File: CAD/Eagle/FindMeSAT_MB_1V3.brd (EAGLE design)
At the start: 99 x 49.2 mm, 137 parts, among them Q101 ABS07-32.768KHZ, Q651 ABM3B-16MHZ-10-R50-1-U, U1001 CFPT-141-20MHZ, U101 ATXMEGA256A3BU-AU, U1011 OPA354, U1021 OPA354, U1111 LM2831YMF, U1121 LM4120IM5-3.0, U201 SIM808, U301 MPU-9250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

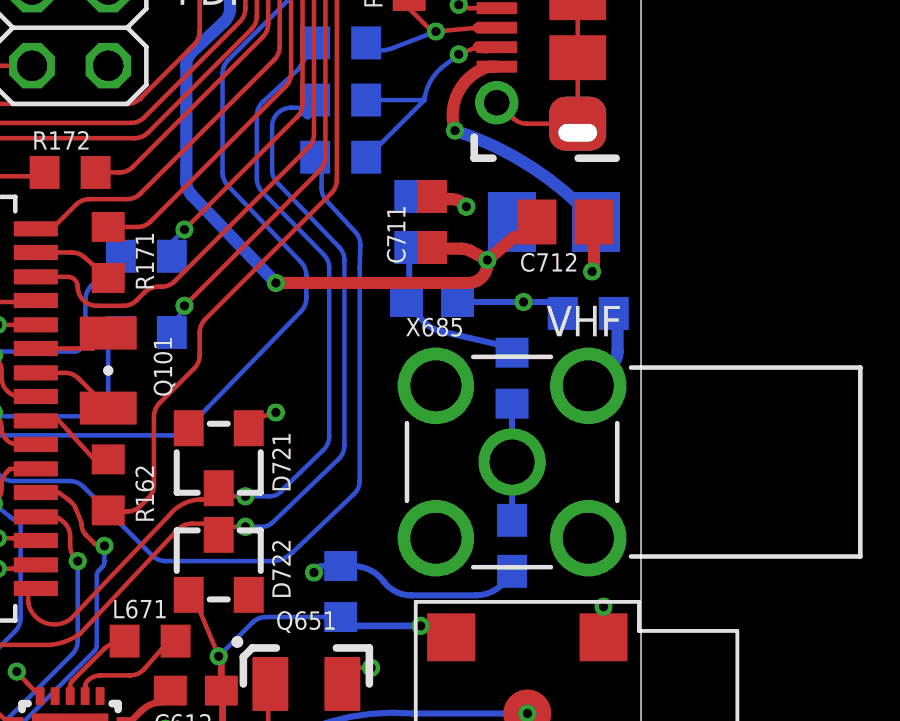
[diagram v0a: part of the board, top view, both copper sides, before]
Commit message: HW_V1.3 - L687 added, AX5243 UHF matching unit enhanced
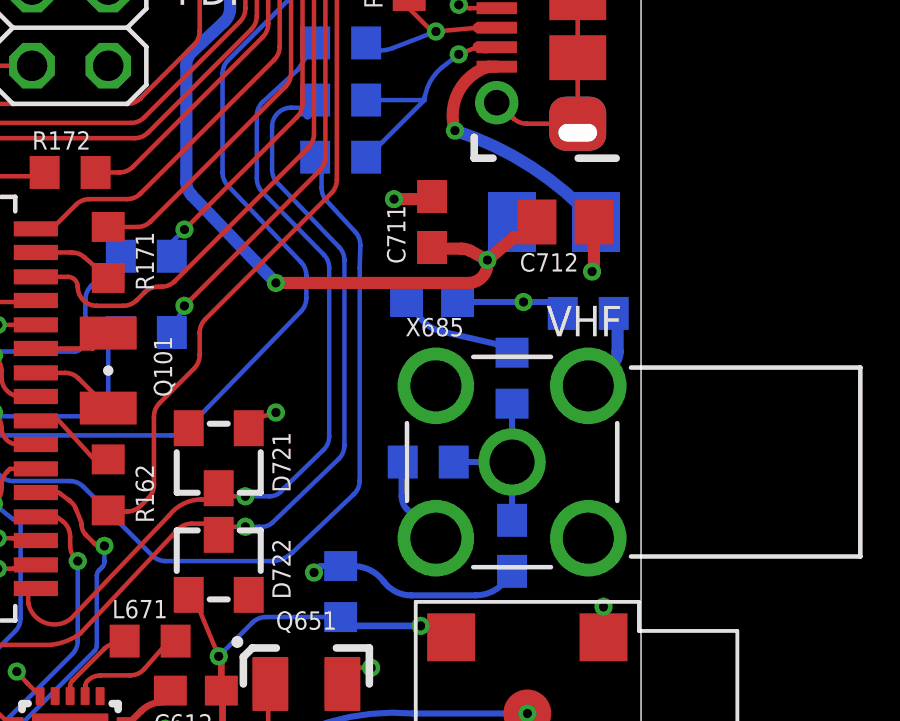
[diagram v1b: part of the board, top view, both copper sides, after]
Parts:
- removed C682: 4.7pF, rcl:C0603
- added L687: 150nH, rcl:R0603
- C681: value 33pF -> 82pF
- C686: value 4.7pF -> 150pF
- L681: value 150nH -> 100nH
- L682: value 22nH -> 56nH
- L686: value 22nH -> 33nH
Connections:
- net AX_ANT: now also L687.2
- net AX_ANT_I: no longer C682.2
- net GND: now also L687.1; no longer C682.1
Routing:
- net AX_ANT: track 3.89 -> 5.83 mm
- net AX_ANT_I: track 5.87 -> 4.14 mm
- net N$5: track 0.00 -> 1.14 mm, vias 0 -> 1
- net GND: track 234.3 -> 233.6 mm, vias 73 -> 72

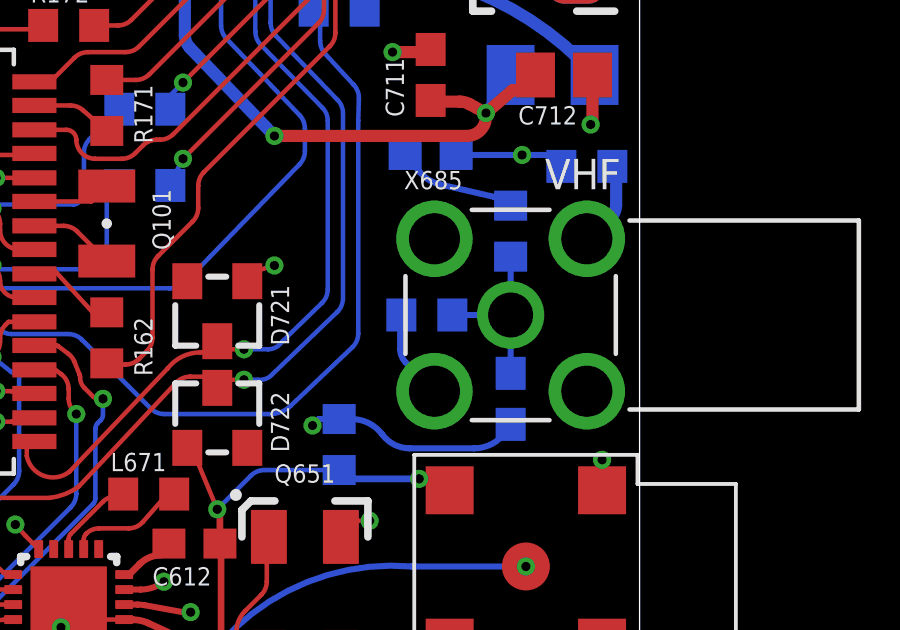
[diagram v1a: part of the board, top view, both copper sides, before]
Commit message: HW_V1.3 - AX5243 - another matching setup
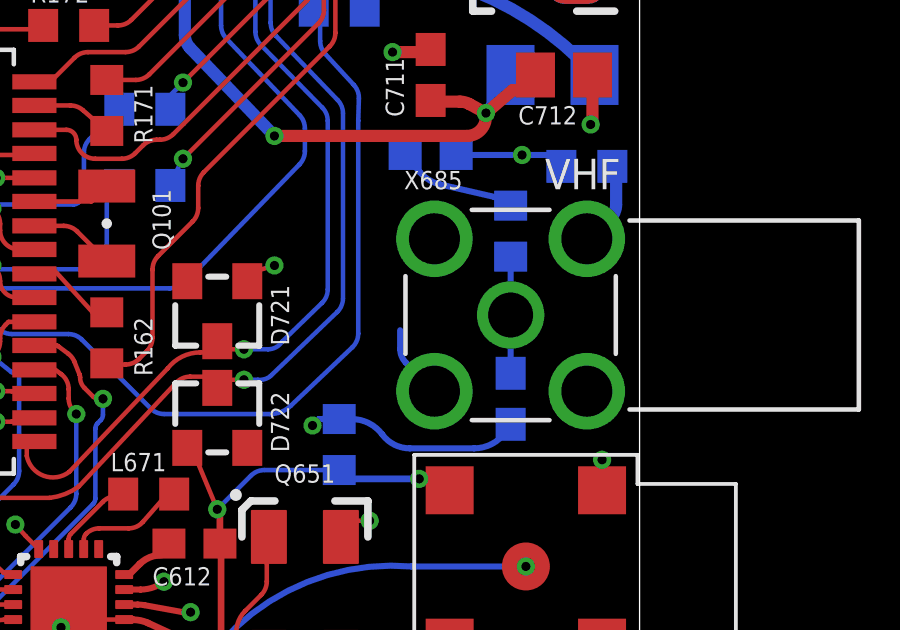
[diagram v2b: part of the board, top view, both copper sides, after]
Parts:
- removed L687: 150nH, rcl:R0603
- C681: value 82pF -> 47pF
- C686: value 150pF -> 3.9pF
- L681: value 100nH -> 150nH
- L682: value 56nH -> 47nH
- L686: value 33nH -> 18nH
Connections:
- net AX_ANT: no longer L687.2
- net GND: no longer L687.1
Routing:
- net AX_ANT: track 5.83 -> 3.89 mm
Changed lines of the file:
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@@
 <attribute name="VALUE" x="81.788" y="7.112" size="0.6096" layer="27"/>
 </element>
-<element name="C681" library="rcl" package="C0603" value="82pF" x="92.075" y="18.796" smashed="yes" rot="MR0">
+<element name="C681" library="rcl" package="C0603" value="47pF" x="92.075" y="18.796" smashed="yes" rot="MR0">
 <attribute name="NAME" x="90.17" y="18.415" size="0.6096" layer="26" rot="MR0"/>
 <attribute name="VALUE" x="92.456" y="18.542" size="0.6096" layer="28" rot="MR0"/>
 </element>
-<element name="L686" library="rcl" package="R0603" value="33nH" x="89.027" y="9.144" smashed="yes" rot="MR90">
+<element name="L686" library="rcl" package="R0603" value="18nH" x="89.027" y="9.144" smashed="yes" rot="MR90">
 <attribute name="NAME" x="88.773" y="5.207" size="0.6096" layer="26" rot="MR90"/>
 <attribute name="VALUE" x="88.773" y="8.001" size="0.6096" layer="28" rot="MR90"/>
 </element>
-<element name="L682" library="rcl" package="R0603" value="56nH" x="94.742" y="16.256" smashed="yes" rot="MR270">
+<element name="L682" library="rcl" package="R0603" value="47nH" x="94.742" y="16.256" smashed="yes" rot="MR270">
 <attribute name="NAME" x="94.488" y="18.034" size="0.6096" layer="26" rot="MR90"/>
 <attribute name="VALUE" x="94.488" y="15.24" size="0.6096" layer="28" rot="MR90"/>
 </element>
-<element name="C686" library="rcl" package="C0603" value="150pF" x="94.742" y="10.668" smashed="yes" rot="MR90">
+<element name="C686" library="rcl" package="C0603" value="3.9pF" x="94.742" y="10.668" smashed="yes" rot="MR90">
 <attribute name="NAME" x="94.488" y="6.604" size="0.6096" layer="26" rot="MR90"/>
 <attribute name="VALUE" x="94.488" y="10.287" size="0.6096" layer="28" rot="MR90"/>
 </element>
-<element name="L681" library="rcl" package="R0603" value="100nH" x="97.282" y="18.415" smashed="yes" rot="MR180">
+<element name="L681" library="rcl" package="R0603" value="150nH" x="97.282" y="18.415" smashed="yes" rot="MR180">
 <attribute name="NAME" x="98.425" y="19.304" size="0.6096" layer="26" rot="MR0"/>
 <attribute name="VALUE" x="98.552" y="18.161" size="0.6096" layer="28" rot="MR0"/>
@@
 <attribute name="VALUE" x="46.355" y="26.162" size="0.6096" layer="27" rot="R270"/>
 </element>
-<element name="L687" library="rcl" package="R0603" value="150nH" x="91.948" y="13.462" rot="MR180"/>
 </elements>
 <signals>
@@
 <wire x1="42.037" y1="14.097" x2="42.037" y2="14.732" width="0.1524" layer="16"/>
 <contactref element="C711" pad="2"/>
-<contactref element="L687" pad="1"/>
+<wire x1="91.059" y1="12.954" x2="91.059" y2="12.328025" width="0.2032" layer="16"/>
+<wire x1="91.059" y1="12.328025" x2="91.2449875" y2="11.8790125" width="0.2032" layer="16" curve="45"/>
+<wire x1="91.2449875" y1="11.8790125" x2="92.202" y2="10.922" width="0.2032" layer="16"/>
 <wire x1="93.384" y1="32.258" x2="94.996" y2="38.1" width="0" layer="19" extent="16-16"/>
 <wire x1="92.075" y1="22.313" x2="93.599" y2="29.337" width="0" layer="19" extent="1-1"/>
@@
 <wire x1="98.132" y1="18.415" x2="97.47" y2="19.751" width="0" layer="19" extent="1-16"/>
 <wire x1="92.202" y1="16.002" x2="97.282" y2="16.002" width="0" layer="19" extent="1-1"/>
-<wire x1="97.282" y1="10.922" x2="97.282" y2="16.002" width="0" layer="19" extent="1-1"/>
-<wire x1="97.79" y1="8.636" x2="97.282" y2="10.922" width="0" layer="19" extent="1-1"/>
-<wire x1="92.202" y1="10.922" x2="92.202" y2="16.002" width="0" layer="19" extent="1-1"/>
+<wire x1="91.059" y1="12.954" x2="92.202" y2="16.002" width="0" layer="19" extent="16-16"/>
 <wire x1="91.694" y1="8.001" x2="92.202" y2="10.922" width="0" layer="19" extent="1-1"/>
 <wire x1="89.408" y1="6.604" x2="89.447" y2="8.001" width="0" layer="19" extent="1-16"/>
@@
 <wire x1="86.684" y1="2.064" x2="85.09" y2="2.54" width="0" layer="19" extent="1-1"/>
 <wire x1="86.995" y1="1.524" x2="86.684" y2="2.064" width="0" layer="19" extent="1-1"/>
+<wire x1="86.868" y1="15.113" x2="91.059" y2="12.954" width="0" layer="19" extent="16-16"/>
 <wire x1="92.71" y1="2.54" x2="90.043" y2="6.604" width="0" layer="19" extent="1-1"/>
-<wire x1="97.79" y1="2.54" x2="97.79" y2="7.62" width="0" layer="19" extent="1-1"/>
+<wire x1="97.282" y1="10.922" x2="97.282" y2="16.002" width="0" layer="19" extent="1-1"/>
+<wire x1="97.79" y1="8.636" x2="97.282" y2="10.922" width="0" layer="19" extent="1-1"/>
+<wire x1="97.79" y1="2.54" x2="92.71" y2="2.54" width="0" layer="19" extent="1-1"/>
 <wire x1="74.422" y1="2.54" x2="79.51" y2="2.532" width="0" layer="19" extent="1-1"/>
 <wire x1="78.867" y1="10.033" x2="83.963" y2="9.033" width="0" layer="19" extent="1-1"/>
-<wire x1="86.868" y1="15.113" x2="92.202" y2="16.002" width="0" layer="19" extent="1-1"/>
 <wire x1="70.866" y1="9.271" x2="76.2" y2="10.58" width="0" layer="19" extent="16-16"/>
 <wire x1="65.913" y1="12.407" x2="70.016" y2="10.668" width="0" layer="19" extent="16-16"/>
@@
 <wire x1="11.43" y1="37.973" x2="11.43" y2="38.1" width="0" layer="19" extent="1-1"/>
 <wire x1="15.66" y1="36.068" x2="15.367" y2="36.068" width="0" layer="19" extent="1-1"/>
-<wire x1="91.098" y1="13.462" x2="4.591059375" y2="1.0096875" width="0" layer="19" extent="1-1"/>
-<wire x1="91.059" y1="12.954" x2="91.059" y2="12.328025" width="0.2032" layer="16"/>
-<wire x1="91.059" y1="12.328025" x2="91.2449875" y2="11.8790125" width="0.2032" layer="16" curve="45"/>
-<wire x1="91.2449875" y1="11.8790125" x2="92.202" y2="10.922" width="0.2032" layer="16"/>
 </signal>
 <signal name="EN">
@@
 <wire x1="94.742" y1="11.518" x2="94.742" y2="13.462" width="0.2032" layer="16"/>
 <wire x1="94.742" y1="15.406" x2="94.742" y2="13.462" width="0.2032" layer="16"/>
-<contactref element="L687" pad="2"/>
-<wire x1="92.798" y1="13.462" x2="94.742" y2="13.462" width="0.2032" layer="16"/>
 </signal>
 <signal name="AX_ANT_I" class="2">
